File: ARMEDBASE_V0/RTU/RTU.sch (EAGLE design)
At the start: 10 parts, among them Q2 2N3904

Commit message: rtu
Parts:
- added C1: 10uf, SparkFun-Capacitors:CAP0805
- added C2: 100uf, SparkFun-Capacitors:CAP0805
- added C3, C4: 22pF, SparkFun-Capacitors:CAP0805
- added C5: 10nF, SparkFun-Capacitors:CAP0805
- added D1: (no value), SparkFun-DiscreteSemi:DIODESMA
- added IC1: REG1117, burr-brown:REG1117
- added IC2: MEGA8-P, atmel:MEGA8-P
- added LED1: (no value), led:LEDCHIP-LED0805
- added LOGO1: OSHW-LOGOL, SparkFun-Aesthetics:OSHW-LOGOL
- added Q1: 20Mhz, crystal:CRYSTALSM49
- added R8: 330, SparkFun-Passives:RESISTOR0805-RES
- added R9: 1K, SparkFun-Passives:RESISTOR0805-RES
- added S1: (no value), switch:255SB
- added S2: SWITCH-MOMENTARY-2PTH, SparkFun-Electromechanical:SWITCH-MOMENTARY-2PTH
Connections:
- new net N$11: LED1.A, R8.1
- new net N$13: D1.A, S1.O
- new net N$21: C3.2, IC2.PB6(XTAL1/TOSC1), Q1.2
- new net N$23: C4.2, IC2.PB7(XTAL2/TOSC2), Q1.1
- new net N$24: C5.2, IC2.PC6(/RESET), R9.2, S2.1
- new net VCC: P&C.4, S1.P
- new net VCC12V: C2.2, D1.C, IC1.VIN
- net GND: now also C1.1, C2.1, C3.1, C4.1, C5.1, IC1.GND, IC2.GND, IC2.GND@1, LED1.C, P&C.3, S2.2
- net RX: now also IC2.PD0(RXD)
- net TX: now also IC2.PD1(TXD)
- net VCC5V: now also C1.2, IC1.VOUT, IC2.AVCC, IC2.VCC@1, R8.2, R9.1
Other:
- moved on the sheet: P&C, Q2, R1, R2, R3, R4, R5, R6, R7, U$1

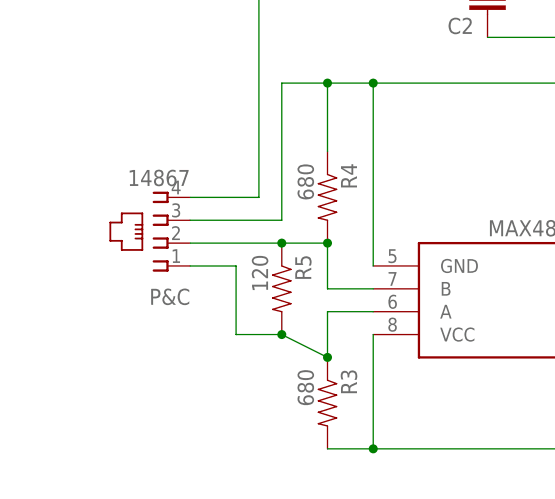
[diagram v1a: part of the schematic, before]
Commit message: modbus in-out
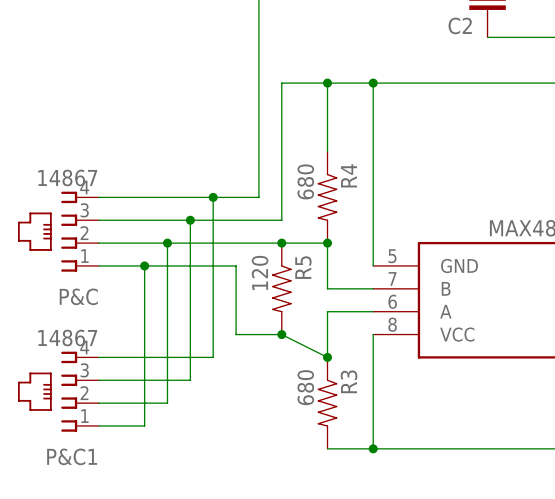
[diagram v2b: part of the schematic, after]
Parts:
- added P&C1: 14867, con-4ucon:14867
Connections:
- net GND: now also P&C1.3
- net N$7: now also P&C1.2
- net N$8: now also P&C1.1
- net VCC: now also P&C1.4
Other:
- moved on the sheet: P&C
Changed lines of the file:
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@@
 <part name="C2" library="SparkFun-Capacitors" deviceset="CAP" device="0805" value="100uf"/>
 <part name="R8" library="SparkFun-Passives" deviceset="RESISTOR" device="0805-RES" value="330"/>
+<part name="P&amp;C1" library="con-4ucon" deviceset="14867" device=""/>
 </parts>
 <sheets>
@@
 <instance part="R1" gate="G$1" x="76.2" y="20.32" rot="R270"/>
 <instance part="Q2" gate="G$1" x="68.58" y="45.72" rot="R180"/>
-<instance part="P&amp;C" gate="G$1" x="12.7" y="40.64" rot="R180"/>
+<instance part="P&amp;C" gate="G$1" x="2.54" y="40.64" rot="R180"/>
 <instance part="U$1" gate="G$1" x="50.8" y="33.02" rot="R180"/>
 <instance part="R2" gate="G$1" x="68.58" y="20.32" rot="R270"/>
@@
 <instance part="C2" gate="G$1" x="48.26" y="66.04" rot="R180"/>
 <instance part="R8" gate="G$1" x="86.36" y="68.58" rot="R90"/>
+<instance part="P&amp;C1" gate="G$1" x="2.54" y="22.86" rot="R180"/>
 </instances>
 <busses>
@@
 <pinref part="GND2" gate="1" pin="GND"/>
 <pinref part="P&amp;C" gate="G$1" pin="3"/>
+<wire x1="5.08" y1="40.64" x2="15.24" y2="40.64" width="0.1524" layer="91"/>
 <wire x1="15.24" y1="40.64" x2="25.4" y2="40.64" width="0.1524" layer="91"/>
 <wire x1="25.4" y1="40.64" x2="25.4" y2="55.88" width="0.1524" layer="91"/>
@@
 <wire x1="76.2" y1="60.96" x2="78.74" y2="60.96" width="0.1524" layer="91"/>
 <wire x1="60.96" y1="60.96" x2="60.96" y2="55.88" width="0.1524" layer="91"/>
+<wire x1="15.24" y1="40.64" x2="15.24" y2="22.86" width="0.1524" layer="91"/>
+<pinref part="P&amp;C1" gate="G$1" pin="3"/>
+<wire x1="15.24" y1="22.86" x2="5.08" y2="22.86" width="0.1524" layer="91"/>
+<junction x="15.24" y="40.64"/>
 </segment>
 <segment>
@@
 <wire x1="35.56" y1="33.02" x2="30.48" y2="33.02" width="0.1524" layer="91"/>
 <wire x1="30.48" y1="33.02" x2="30.48" y2="38.1" width="0.1524" layer="91"/>
-<wire x1="25.4" y1="38.1" x2="15.24" y2="38.1" width="0.1524" layer="91"/>
+<wire x1="25.4" y1="38.1" x2="12.7" y2="38.1" width="0.1524" layer="91"/>
 <pinref part="P&amp;C" gate="G$1" pin="2"/>
 <junction x="25.4" y="38.1"/>
+<wire x1="12.7" y1="38.1" x2="5.08" y2="38.1" width="0.1524" layer="91"/>
+<wire x1="12.7" y1="38.1" x2="12.7" y2="20.32" width="0.1524" layer="91"/>
+<pinref part="P&amp;C1" gate="G$1" pin="2"/>
+<wire x1="12.7" y1="20.32" x2="5.08" y2="20.32" width="0.1524" layer="91"/>
+<junction x="12.7" y="38.1"/>
 </segment>
 </net>
@@
 <junction x="30.48" y="25.4"/>
 <pinref part="P&amp;C" gate="G$1" pin="1"/>
-<wire x1="15.24" y1="35.56" x2="20.32" y2="35.56" width="0.1524" layer="91"/>
+<wire x1="5.08" y1="35.56" x2="10.16" y2="35.56" width="0.1524" layer="91"/>
+<wire x1="10.16" y1="35.56" x2="20.32" y2="35.56" width="0.1524" layer="91"/>
 <wire x1="20.32" y1="35.56" x2="20.32" y2="27.94" width="0.1524" layer="91"/>
 <junction x="25.4" y="27.94"/>
+<wire x1="10.16" y1="35.56" x2="10.16" y2="17.78" width="0.1524" layer="91"/>
+<pinref part="P&amp;C1" gate="G$1" pin="1"/>
+<wire x1="10.16" y1="17.78" x2="5.08" y2="17.78" width="0.1524" layer="91"/>
+<junction x="10.16" y="35.56"/>
 </segment>
 </net>
@@
 <pinref part="P&amp;C" gate="G$1" pin="4"/>
 <wire x1="22.86" y1="71.12" x2="27.94" y2="71.12" width="0.1524" layer="91"/>
-<wire x1="15.24" y1="43.18" x2="22.86" y2="43.18" width="0.1524" layer="91"/>
+<wire x1="5.08" y1="43.18" x2="17.78" y2="43.18" width="0.1524" layer="91"/>
+<wire x1="17.78" y1="43.18" x2="22.86" y2="43.18" width="0.1524" layer="91"/>
 <wire x1="17.78" y1="71.12" x2="22.86" y2="71.12" width="0.1524" layer="91"/>
 <wire x1="22.86" y1="71.12" x2="22.86" y2="43.18" width="0.1524" layer="91"/>
-</segment>
-</net>
+<wire x1="17.78" y1="43.18" x2="17.78" y2="25.4" width="0.1524" layer="91"/>
+<pinref part="P&amp;C1" gate="G$1" pin="4"/>
+<wire x1="17.78" y1="25.4" x2="5.08" y2="25.4" width="0.1524" layer="91"/>
+<junction x="17.78" y="43.18"/>
+</segment>
+</net>

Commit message: MCU almost
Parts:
- added F1: 100mA, special:FUSE
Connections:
- new net N$9: C1.2, F1.1, IC1.VOUT, R8.2
- net VCC5V: now also F1.2; no longer C1.2, IC1.VOUT, R8.2
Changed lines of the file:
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@@
 <part name="R8" library="SparkFun-Passives" deviceset="RESISTOR" device="0805-RES" value="330"/>
 <part name="P&amp;C1" library="con-4ucon" deviceset="14867" device=""/>
+<part name="F1" library="special" deviceset="FUSE" device="" value="100mA"/>
 </parts>
 <sheets>
@@
 <instance part="R8" gate="G$1" x="86.36" y="68.58" rot="R90"/>
 <instance part="P&amp;C1" gate="G$1" x="2.54" y="22.86" rot="R180"/>
+<instance part="F1" gate="G$1" x="99.06" y="73.66"/>
 </instances>
 <busses>
@@
 </segment>
 <segment>
-<pinref part="IC1" gate="G$1" pin="VOUT"/>
-<wire x1="73.66" y1="73.66" x2="76.2" y2="73.66" width="0.1524" layer="91"/>
-<pinref part="C1" gate="G$1" pin="2"/>
-<wire x1="76.2" y1="73.66" x2="76.2" y2="68.58" width="0.1524" layer="91"/>
-<wire x1="76.2" y1="73.66" x2="86.36" y2="73.66" width="0.1524" layer="91"/>
-<pinref part="R8" gate="G$1" pin="2"/>
-<wire x1="86.36" y1="73.66" x2="96.52" y2="73.66" width="0.1524" layer="91"/>
-<junction x="86.36" y="73.66"/>
-<junction x="76.2" y="73.66"/>
-<label x="96.52" y="73.66" size="1.778" layer="95" xref="yes"/>
+<pinref part="F1" gate="G$1" pin="2"/>
+<wire x1="104.14" y1="73.66" x2="109.22" y2="73.66" width="0.1524" layer="91"/>
+<label x="109.22" y="73.66" size="1.778" layer="95" xref="yes"/>
 </segment>
 </net>
@@
 <junction x="48.26" y="73.66"/>
 <wire x1="48.26" y1="73.66" x2="48.26" y2="83.82" width="0.1524" layer="91"/>
-<wire x1="48.26" y1="83.82" x2="96.52" y2="83.82" width="0.1524" layer="91"/>
-<label x="96.52" y="83.82" size="1.778" layer="95" xref="yes"/>
+<wire x1="48.26" y1="83.82" x2="109.22" y2="83.82" width="0.1524" layer="91"/>
+<label x="109.22" y="83.82" size="1.778" layer="95" xref="yes"/>
 </segment>
 </net>
@@
 </segment>
 </net>
+<net name="N$9" class="0">
+<segment>
+<pinref part="IC1" gate="G$1" pin="VOUT"/>
+<wire x1="73.66" y1="73.66" x2="76.2" y2="73.66" width="0.1524" layer="91"/>
+<pinref part="C1" gate="G$1" pin="2"/>
+<wire x1="76.2" y1="73.66" x2="76.2" y2="68.58" width="0.1524" layer="91"/>
+<wire x1="76.2" y1="73.66" x2="86.36" y2="73.66" width="0.1524" layer="91"/>
+<pinref part="R8" gate="G$1" pin="2"/>
+<wire x1="86.36" y1="73.66" x2="91.44" y2="73.66" width="0.1524" layer="91"/>
+<junction x="86.36" y="73.66"/>
+<junction x="76.2" y="73.66"/>
+<pinref part="F1" gate="G$1" pin="1"/>
+</segment>
+</net>

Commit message: rtu fuse
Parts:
- F1: value 100mA -> 100ma; device special:FUSE -> _hhn_PtcFuses_Siba_r500_Ozan:SIBA194600
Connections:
- net N$9: now also F1.2, IC1.VIN; no longer C1.2, F1.1, IC1.VOUT, R8.2
- net VCC12V: now also F1.1; no longer IC1.VIN
- net VCC5V: now also C1.2, IC1.VOUT, R8.2; no longer F1.2
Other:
- moved on the sheet: C1, IC1, LED1, R8
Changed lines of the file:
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@@
 </variantdefs>
 <classes>
-<class number="0" name="default" width="0" drill="0">
+<class number="0" name="default" width="0.3" drill="0.5">
+<clearance class="0" value="0.25"/>
 </class>
 </classes>
@@
 <part name="R8" library="SparkFun-Passives" deviceset="RESISTOR" device="0805-RES" value="330"/>
 <part name="P&amp;C1" library="con-4ucon" deviceset="14867" device=""/>
-<part name="F1" library="special" deviceset="FUSE" device="" value="100mA"/>
+<part name="F1" library="_hhn_PtcFuses_Siba_r500_Ozan" deviceset="SIBA194600*" device="" value="100ma"/>
 </parts>
 <sheets>
@@
 <instance part="LOGO1" gate="G$1" x="134.62" y="22.86"/>
 <instance part="S2" gate="G$1" x="137.16" y="76.2"/>
-<instance part="IC1" gate="G$1" x="60.96" y="73.66"/>
-<instance part="C1" gate="G$1" x="76.2" y="66.04" rot="R180"/>
-<instance part="LED1" gate="G$1" x="83.82" y="60.96" rot="R270"/>
+<instance part="IC1" gate="G$1" x="76.2" y="73.66"/>
+<instance part="C1" gate="G$1" x="91.44" y="66.04" rot="R180"/>
+<instance part="LED1" gate="G$1" x="99.06" y="60.96" rot="R270"/>
 <instance part="D1" gate="G$1" x="43.18" y="73.66"/>
 <instance part="SUPPLY1" gate="G$1" x="17.78" y="71.12" rot="R90"/>
 <instance part="S1" gate="1" x="33.02" y="73.66" rot="R270"/>
 <instance part="C2" gate="G$1" x="48.26" y="66.04" rot="R180"/>
-<instance part="R8" gate="G$1" x="86.36" y="68.58" rot="R90"/>
+<instance part="R8" gate="G$1" x="101.6" y="68.58" rot="R90"/>
 <instance part="P&amp;C1" gate="G$1" x="2.54" y="22.86" rot="R180"/>
-<instance part="F1" gate="G$1" x="99.06" y="73.66"/>
+<instance part="F1" gate="G$1" x="55.88" y="73.66"/>
 </instances>
 <busses>
@@
 </segment>
 <segment>
-<pinref part="F1" gate="G$1" pin="2"/>
-<wire x1="104.14" y1="73.66" x2="109.22" y2="73.66" width="0.1524" layer="91"/>
 <label x="109.22" y="73.66" size="1.778" layer="95" xref="yes"/>
+<pinref part="IC1" gate="G$1" pin="VOUT"/>
+<wire x1="88.9" y1="73.66" x2="91.44" y2="73.66" width="0.1524" layer="91"/>
+<pinref part="C1" gate="G$1" pin="2"/>
+<wire x1="91.44" y1="73.66" x2="91.44" y2="68.58" width="0.1524" layer="91"/>
+<wire x1="91.44" y1="73.66" x2="101.6" y2="73.66" width="0.1524" layer="91"/>
+<pinref part="R8" gate="G$1" pin="2"/>
+<junction x="101.6" y="73.66"/>
+<junction x="91.44" y="73.66"/>
+<wire x1="109.22" y1="73.66" x2="101.6" y2="73.66" width="0.1524" layer="91"/>
 </segment>
 </net>
 <net name="GND" class="0">
 <segment>
-<pinref part="Q2" gate="G$1" pin="E"/>
-<wire x1="66.04" y1="50.8" x2="66.04" y2="55.88" width="0.1524" layer="91"/>
 <pinref part="R7" gate="G$1" pin="1"/>
-<wire x1="66.04" y1="55.88" x2="83.82" y2="55.88" width="0.1524" layer="91"/>
+<wire x1="76.2" y1="55.88" x2="83.82" y2="55.88" width="0.1524" layer="91"/>
 <wire x1="83.82" y1="55.88" x2="88.9" y2="55.88" width="0.1524" layer="91"/>
 <junction x="83.82" y="55.88"/>
-<junction x="66.04" y="55.88"/>
-<wire x1="66.04" y1="55.88" x2="60.96" y2="55.88" width="0.1524" layer="91"/>
 <pinref part="U$1" gate="G$1" pin="GND"/>
-<wire x1="60.96" y1="55.88" x2="35.56" y2="55.88" width="0.1524" layer="91"/>
+<wire x1="76.2" y1="55.88" x2="66.04" y2="55.88" width="0.1524" layer="91"/>
+<wire x1="66.04" y1="55.88" x2="35.56" y2="55.88" width="0.1524" layer="91"/>
 <wire x1="35.56" y1="35.56" x2="35.56" y2="55.88" width="0.1524" layer="91"/>
 <junction x="35.56" y="55.88"/>
@@
 <pinref part="C2" gate="G$1" pin="1"/>
 <pinref part="IC1" gate="G$1" pin="GND"/>
-<wire x1="48.26" y1="60.96" x2="60.96" y2="60.96" width="0.1524" layer="91"/>
+<wire x1="48.26" y1="60.96" x2="76.2" y2="60.96" width="0.1524" layer="91"/>
 <pinref part="C1" gate="G$1" pin="1"/>
+<junction x="91.44" y="60.96"/>
+<wire x1="91.44" y1="60.96" x2="76.2" y2="60.96" width="0.1524" layer="91"/>
 <junction x="76.2" y="60.96"/>
-<wire x1="76.2" y1="60.96" x2="60.96" y2="60.96" width="0.1524" layer="91"/>
-<junction x="60.96" y="60.96"/>
 <pinref part="LED1" gate="G$1" pin="C"/>
-<wire x1="76.2" y1="60.96" x2="78.74" y2="60.96" width="0.1524" layer="91"/>
-<wire x1="60.96" y1="60.96" x2="60.96" y2="55.88" width="0.1524" layer="91"/>
+<wire x1="91.44" y1="60.96" x2="93.98" y2="60.96" width="0.1524" layer="91"/>
+<wire x1="76.2" y1="60.96" x2="76.2" y2="55.88" width="0.1524" layer="91"/>
 <wire x1="15.24" y1="40.64" x2="15.24" y2="22.86" width="0.1524" layer="91"/>
 <pinref part="P&amp;C1" gate="G$1" pin="3"/>
 <wire x1="15.24" y1="22.86" x2="5.08" y2="22.86" width="0.1524" layer="91"/>
 <junction x="15.24" y="40.64"/>
+<pinref part="Q2" gate="G$1" pin="E"/>
+<wire x1="66.04" y1="50.8" x2="66.04" y2="55.88" width="0.1524" layer="91"/>
+<junction x="66.04" y="55.88"/>
 </segment>
 <segment>
@@
 <segment>
 <pinref part="D1" gate="G$1" pin="C"/>
-<pinref part="IC1" gate="G$1" pin="VIN"/>
 <wire x1="45.72" y1="73.66" x2="48.26" y2="73.66" width="0.1524" layer="91"/>
 <pinref part="C2" gate="G$1" pin="2"/>
-<wire x1="48.26" y1="73.66" x2="48.26" y2="68.58" width="0.1524" layer="91"/>
-<junction x="48.26" y="73.66"/>
-<wire x1="48.26" y1="73.66" x2="48.26" y2="83.82" width="0.1524" layer="91"/>
+<wire x1="48.26" y1="73.66" x2="50.8" y2="73.66" width="0.1524" layer="91"/>
 <wire x1="48.26" y1="83.82" x2="109.22" y2="83.82" width="0.1524" layer="91"/>
 <label x="109.22" y="83.82" size="1.778" layer="95" xref="yes"/>
+<wire x1="48.26" y1="83.82" x2="48.26" y2="73.66" width="0.1524" layer="91"/>
+<wire x1="48.26" y1="68.58" x2="48.26" y2="73.66" width="0.1524" layer="91"/>
+<junction x="48.26" y="73.66"/>
+<pinref part="F1" gate="G$1" pin="1"/>
 </segment>
 </net>
@@
 <pinref part="R8" gate="G$1" pin="1"/>
 <pinref part="LED1" gate="G$1" pin="A"/>
-<wire x1="86.36" y1="60.96" x2="86.36" y2="63.5" width="0.1524" layer="91"/>
+<wire x1="101.6" y1="60.96" x2="101.6" y2="63.5" width="0.1524" layer="91"/>
 </segment>
 </net>
@@
 <net name="N$9" class="0">
 <segment>
-<pinref part="IC1" gate="G$1" pin="VOUT"/>
-<wire x1="73.66" y1="73.66" x2="76.2" y2="73.66" width="0.1524" layer="91"/>
-<pinref part="C1" gate="G$1" pin="2"/>
-<wire x1="76.2" y1="73.66" x2="76.2" y2="68.58" width="0.1524" layer="91"/>
-<wire x1="76.2" y1="73.66" x2="86.36" y2="73.66" width="0.1524" layer="91"/>
-<pinref part="R8" gate="G$1" pin="2"/>
-<wire x1="86.36" y1="73.66" x2="91.44" y2="73.66" width="0.1524" layer="91"/>
-<junction x="86.36" y="73.66"/>
-<junction x="76.2" y="73.66"/>
-<pinref part="F1" gate="G$1" pin="1"/>
-</segment>
-</net>
+<pinref part="IC1" gate="G$1" pin="VIN"/>
+<wire x1="60.96" y1="73.66" x2="63.5" y2="73.66" width="0.1524" layer="91"/>
+<pinref part="F1" gate="G$1" pin="2"/>
+</segment>
+</net>
